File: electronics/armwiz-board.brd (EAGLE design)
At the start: 98.8 x 51 mm, 85 parts, among them IC1 MCP3424, J1 SD_MICRO_SDIO_1BIT, J2 CORTEX_DEBUGSMD, U1 STM32F10XRXT6, U4 MIC5219-3.3V, X2 M12_BOTTOM_CONTACTS_FPC_1MM, Y1 32.768kHz, Y3 32.768kHz

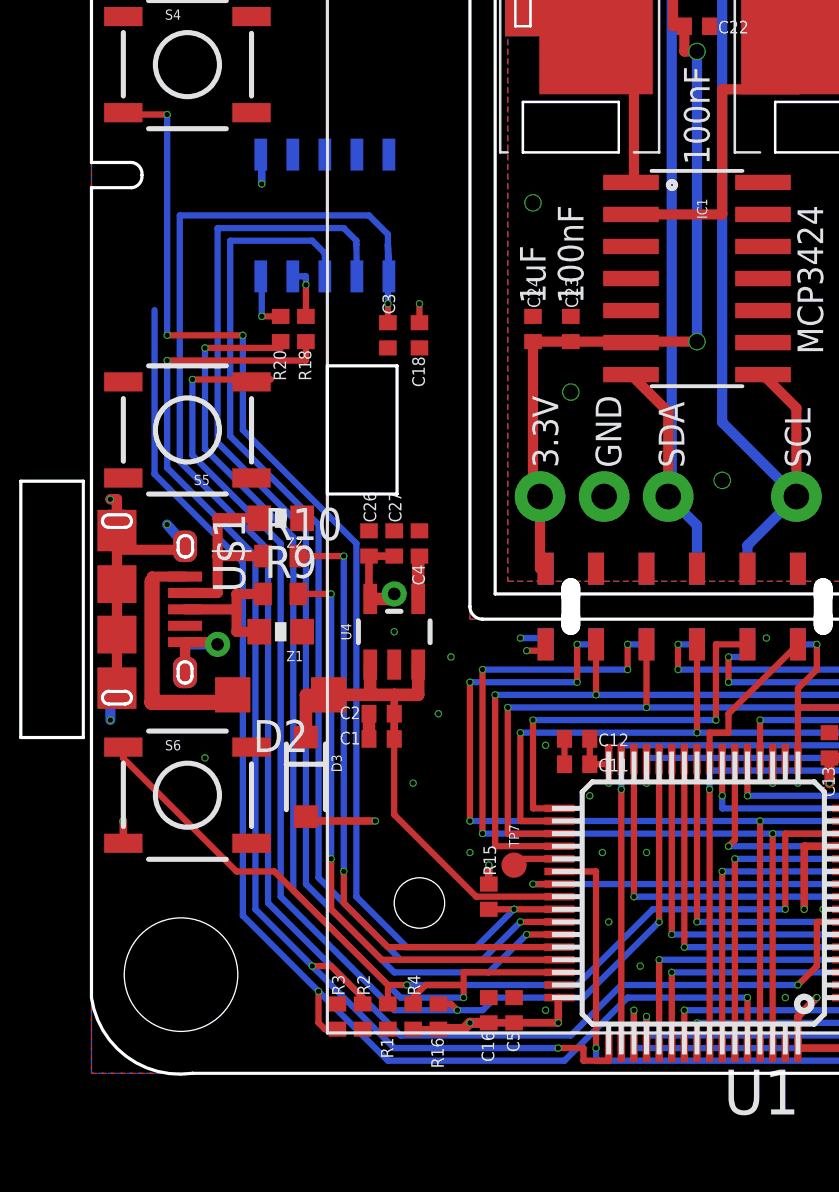
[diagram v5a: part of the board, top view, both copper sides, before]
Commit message: Changed serial pins on Cortex header. Added SWO to Cortex header. Added TODO notes to schematic.
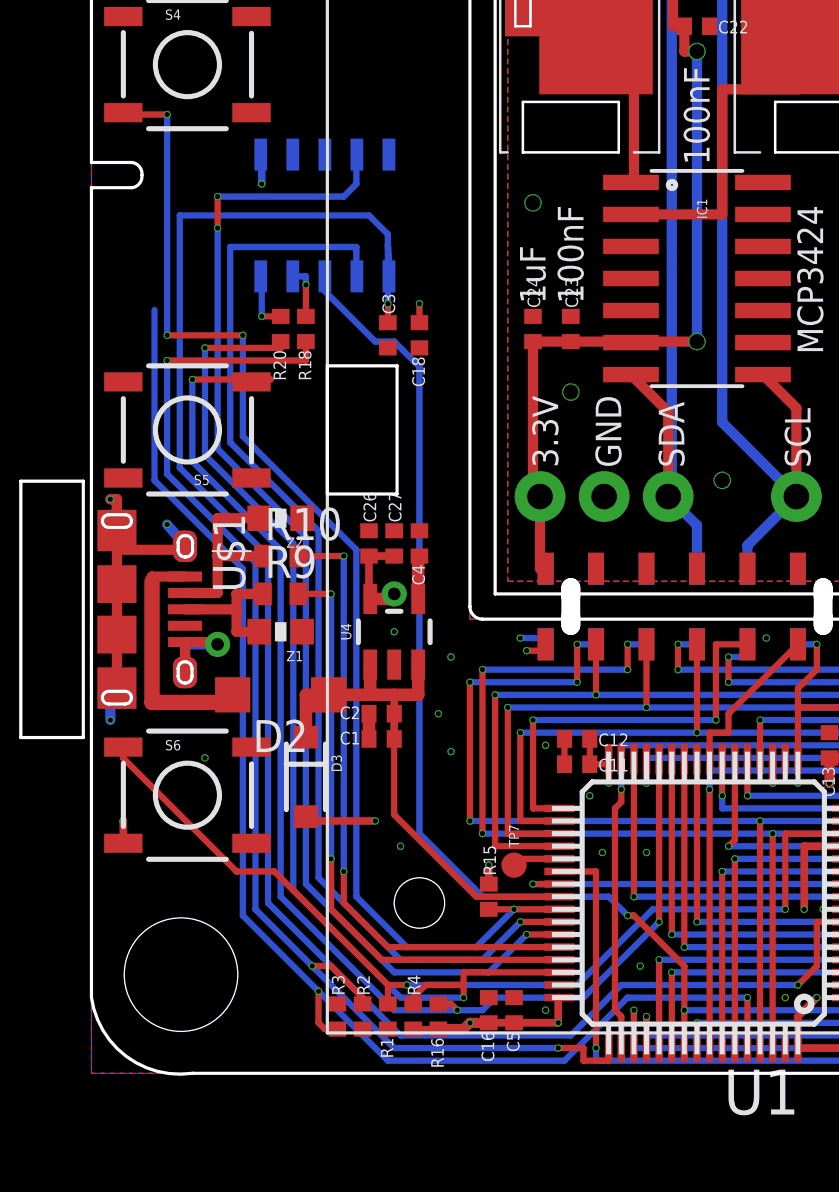
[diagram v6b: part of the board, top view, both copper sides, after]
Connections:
- removed net LCD_SCK_(SPI3_SCK): U1.55, X2.7
- new net LCD_SCK_(SPI3_SCK_SWO): J2.6, U1.55, X2.7
- net USART1_RX: now also J2.7; no longer J2.8
- net USART1_TX: now also J2.8; no longer J2.6
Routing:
- net LCD_SCK_(SPI3_SCK_SWO): track 0.00 -> 75.8 mm, vias 0 -> 3
- net LCD_SCK_(SPI3_SCK): track 37.2 -> 0.00 mm, vias 2 -> 0
- net USART1_TX: track 43.1 -> 44.1 mm
- net USART1_RX: track 46.7 -> 47.7 mm, vias 1 -> 3
- net GND: vias 83 -> 82
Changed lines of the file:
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@@
 <wire x1="11" y1="14.25" x2="11" y2="13.25" width="0.5" layer="1"/>
 <via x="21.75" y="4.25" extent="1-16" drill="0.2"/>
-<via x="20.5" y="6" extent="1-16" drill="0.2"/>
-<via x="12.75" y="11.5" extent="1-16" drill="0.2"/>
+<via x="14.25" y="12.75" extent="1-16" drill="0.2"/>
 <via x="18" y="2.5" extent="1-16" drill="0.2"/>
 <contactref element="R3" pad="1"/>
@@
 <via x="84.5" y="40.5" extent="1-16" drill="0.2"/>
 <via x="89.25" y="43.75" extent="1-16" drill="0.2"/>
-<via x="15" y="8.75" extent="1-16" drill="0.2"/>
+<via x="12.25" y="9" extent="1-16" drill="0.2"/>
 <via x="13.75" y="14.25" extent="1-16" drill="0.2"/>
 <via x="12" y="17.5" extent="1-16" drill="0.2"/>
@@
 <contactref element="S4" pad="3"/>
 <contactref element="U1" pad="41"/>
-<wire x1="10.5" y1="7" x2="10.5" y2="21" width="0.25" layer="16"/>
-<wire x1="10.5" y1="21" x2="6" y2="25.5" width="0.25" layer="16"/>
-<wire x1="6" y1="25.5" x2="6" y2="29.25" width="0.25" layer="16"/>
+<wire x1="10.5" y1="7" x2="10.5" y2="20.75" width="0.25" layer="16"/>
+<wire x1="10.5" y1="20.75" x2="6" y2="25.25" width="0.25" layer="16"/>
+<wire x1="6" y1="25.25" x2="6" y2="29.25" width="0.25" layer="16"/>
 <wire x1="18.55" y1="6.5" x2="16.75" y2="6.5" width="0.25" layer="1"/>
 <via x="16.75" y="6.5" extent="1-16" drill="0.2"/>
@@
 <wire x1="19" y1="1.5" x2="12.25" y2="1.5" width="0.25" layer="16"/>
 <wire x1="12.25" y1="1.5" x2="7" y2="6.75" width="0.25" layer="16"/>
-<wire x1="7" y1="6.75" x2="7" y2="20.75" width="0.25" layer="16"/>
-<wire x1="7" y1="20.75" x2="3.5" y2="24.25" width="0.25" layer="16"/>
-<wire x1="3.5" y1="24.25" x2="3.5" y2="34" width="0.25" layer="16"/>
+<wire x1="7" y1="6.75" x2="7" y2="20.5" width="0.25" layer="16"/>
+<wire x1="7" y1="20.5" x2="3.5" y2="24" width="0.25" layer="16"/>
+<wire x1="3.5" y1="24" x2="3.5" y2="34" width="0.25" layer="16"/>
 <wire x1="11.75" y1="29.75" x2="11.75" y2="30.5" width="0.25" layer="1"/>
 <via x="11.75" y="30.5" extent="1-16" drill="0.2"/>
@@
 <wire x1="14.75" y1="3" x2="12.25" y2="3" width="0.25" layer="16"/>
 <wire x1="12.25" y1="3" x2="8" y2="7.25" width="0.25" layer="16"/>
-<wire x1="8" y1="7.25" x2="8" y2="21.25" width="0.25" layer="16"/>
-<wire x1="8" y1="21.25" x2="4.5" y2="24.75" width="0.25" layer="16"/>
-<wire x1="4.5" y1="24.75" x2="4.5" y2="28.75" width="0.25" layer="16"/>
+<wire x1="8" y1="7.25" x2="8" y2="21" width="0.25" layer="16"/>
+<wire x1="8" y1="21" x2="4.5" y2="24.5" width="0.25" layer="16"/>
+<wire x1="4.5" y1="24.5" x2="4.5" y2="28.75" width="0.25" layer="16"/>
 <via x="4.5" y="28.75" extent="1-16" drill="0.2"/>
 <wire x1="12.75" y1="2.75" x2="12.75" y2="3" width="0.25" layer="1"/>
@@
 <wire x1="15.5" y1="4.5" x2="12.25" y2="4.5" width="0.25" layer="16"/>
 <wire x1="12.25" y1="4.5" x2="9" y2="7.75" width="0.25" layer="16"/>
-<wire x1="9" y1="7.75" x2="9" y2="21.75" width="0.25" layer="16"/>
-<wire x1="9" y1="21.75" x2="5.5" y2="25.25" width="0.25" layer="16"/>
-<wire x1="5.5" y1="25.25" x2="5.5" y2="33" width="0.25" layer="16"/>
+<wire x1="9" y1="7.75" x2="9" y2="21.5" width="0.25" layer="16"/>
+<wire x1="9" y1="21.5" x2="5.5" y2="25" width="0.25" layer="16"/>
+<wire x1="5.5" y1="25" x2="5.5" y2="32.75" width="0.25" layer="16"/>
 <via x="17" y="6" extent="1-16" drill="0.2"/>
-<contactref element="J2" pad="6"/>
-<wire x1="5.5" y1="33" x2="8.75" y2="33" width="0.25" layer="16"/>
-<wire x1="8.75" y1="33" x2="9.25" y2="32.5" width="0.25" layer="16"/>
-<wire x1="9.25" y1="32.5" x2="9.25" y2="31.587" width="0.25" layer="16"/>
+<contactref element="J2" pad="8"/>
+<wire x1="5.5" y1="32.75" x2="10.5" y2="32.75" width="0.254" layer="16"/>
+<wire x1="10.5" y1="32.75" x2="10.5" y2="31.607" width="0.254" layer="16"/>
+<wire x1="10.5" y1="31.607" x2="10.52" y2="31.587" width="0.254" layer="16"/>
 </signal>
 <signal name="USART1_RX">
@@
 <wire x1="15.75" y1="4" x2="12" y2="4" width="0.25" layer="16"/>
 <wire x1="12" y1="4" x2="8.5" y2="7.5" width="0.25" layer="16"/>
-<wire x1="8.5" y1="7.5" x2="8.5" y2="21.5" width="0.25" layer="16"/>
-<wire x1="8.5" y1="21.5" x2="5" y2="25" width="0.25" layer="16"/>
-<wire x1="5" y1="25" x2="5" y2="33.5" width="0.25" layer="16"/>
+<wire x1="8.5" y1="7.5" x2="8.5" y2="21.25" width="0.25" layer="16"/>
+<wire x1="8.5" y1="21.25" x2="5" y2="24.75" width="0.25" layer="16"/>
+<wire x1="5" y1="24.75" x2="5" y2="33.5" width="0.25" layer="16"/>
 <via x="17.25" y="5.5" extent="1-16" drill="0.2"/>
-<contactref element="J2" pad="8"/>
-<wire x1="5" y1="33.5" x2="10" y2="33.5" width="0.25" layer="16"/>
-<wire x1="10" y1="33.5" x2="10.5" y2="33" width="0.25" layer="16"/>
-<wire x1="10.5" y1="33" x2="10.5" y2="32.837" width="0.25" layer="16"/>
-<wire x1="10.5" y1="32.837" x2="10.52" y2="31.587" width="0.25" layer="16"/>
+<contactref element="J2" pad="7"/>
+<via x="5" y="33.5" extent="1-16" drill="0.2"/>
+<wire x1="5" y1="33.5" x2="5" y2="34.75" width="0.254" layer="1"/>
+<via x="5" y="34.75" extent="1-16" drill="0.2"/>
+<wire x1="5" y1="34.75" x2="10" y2="34.75" width="0.254" layer="16"/>
+<wire x1="10" y1="34.75" x2="10.5" y2="35.25" width="0.254" layer="16"/>
+<wire x1="10.5" y1="35.25" x2="10.5" y2="36.393" width="0.254" layer="16"/>
+<wire x1="10.5" y1="36.393" x2="10.52" y2="36.413" width="0.254" layer="16"/>
 </signal>
 <signal name="N$13">
@@
 <wire x1="38" y1="16.5" x2="38.75" y2="16.5" width="0.25" layer="16"/>
 </signal>
-<signal name="LCD_SCK_(SPI3_SCK)">
+<signal name="LCD_SCK_(SPI3_SCK_SWO)">
 <contactref element="U1" pad="55"/>
 <wire x1="23.5" y1="2.5" x2="48.5" y2="2.5" width="0.25" layer="16"/>
@@
 <wire x1="23.5" y1="1.05" x2="23.5" y2="2.5" width="0.25" layer="1"/>
 <via x="23.5" y="2.5" extent="1-16" drill="0.2"/>
+<contactref element="J2" pad="6"/>
+<wire x1="23.5" y1="2.5" x2="23.5" y2="4.25" width="0.254" layer="1"/>
+<wire x1="23.5" y1="4.25" x2="21.5" y2="6.25" width="0.254" layer="1"/>
+<wire x1="21.5" y1="6.25" x2="21.25" y2="6.25" width="0.254" layer="1"/>
+<wire x1="9.25" y1="31.587" x2="9.25" y2="31" width="0.254" layer="16"/>
+<wire x1="9.25" y1="31" x2="11.25" y2="29" width="0.254" layer="16"/>
+<wire x1="11.25" y1="29" x2="12" y2="29" width="0.254" layer="16"/>
+<wire x1="12" y1="29" x2="13" y2="28" width="0.254" layer="16"/>
+<wire x1="13" y1="28" x2="13" y2="9.5" width="0.254" layer="16"/>
+<wire x1="13" y1="9.5" x2="15.5" y2="7" width="0.254" layer="16"/>
+<wire x1="15.5" y1="7" x2="20.5" y2="7" width="0.254" layer="16"/>
+<wire x1="20.5" y1="7" x2="21.25" y2="6.25" width="0.254" layer="16"/>
+<via x="21.25" y="6.25" extent="1-16" drill="0.2"/>
 </signal>
 <signal name="LCD_MOSI_(SPI3_MOSI)">
@@
 <wire x1="12" y1="1" x2="8.75" y2="4.25" width="0.25" layer="16"/>
 <wire x1="8.75" y1="4.25" x2="6.5" y2="6.5" width="0.25" layer="16"/>
-<wire x1="6.5" y1="6.5" x2="6.5" y2="20.5" width="0.25" layer="16"/>
-<wire x1="6.5" y1="20.5" x2="3" y2="24" width="0.25" layer="16"/>
-<wire x1="3" y1="24" x2="3" y2="28.25" width="0.25" layer="16"/>
+<wire x1="6.5" y1="6.5" x2="6.5" y2="20.25" width="0.25" layer="16"/>
+<wire x1="6.5" y1="20.25" x2="3" y2="23.75" width="0.25" layer="16"/>
+<wire x1="3" y1="23.75" x2="3" y2="28.25" width="0.25" layer="16"/>
 <via x="3" y="28.25" extent="1-16" drill="0.2"/>
 <wire x1="8.5" y1="28.25" x2="8.5" y2="29" width="0.25" layer="1"/>
@@
 <signal name="LCD_CS_(SPI3_NSS)">
 <contactref element="U1" pad="50"/>
-<wire x1="21" y1="1.05" x2="21" y2="11.25" width="0.25" layer="1"/>
+<wire x1="21" y1="1.05" x2="21" y2="2.25" width="0.25" layer="1"/>
+<wire x1="21" y1="2.25" x2="20.75" y2="2.5" width="0.25" layer="1"/>
+<wire x1="20.75" y1="2.5" x2="20.75" y2="10.5" width="0.25" layer="1"/>
+<wire x1="20.75" y1="10.5" x2="21" y2="10.75" width="0.25" layer="1"/>
+<wire x1="21" y1="10.75" x2="21" y2="11.25" width="0.25" layer="1"/>
 <via x="21" y="11.25" extent="1-16" drill="0.2"/>
 <via x="51.5" y="12" extent="1-16" drill="0.2"/>
@@
 <wire x1="14.5" y1="2.5" x2="12" y2="2.5" width="0.25" layer="16"/>
 <wire x1="12" y1="2.5" x2="7.5" y2="7" width="0.25" layer="16"/>
-<wire x1="7.5" y1="7" x2="7.5" y2="21" width="0.25" layer="16"/>
-<wire x1="7.5" y1="21" x2="4" y2="24.5" width="0.25" layer="16"/>
-<wire x1="4" y1="24.5" x2="4" y2="27.5" width="0.25" layer="16"/>
+<wire x1="7.5" y1="7" x2="7.5" y2="20.75" width="0.25" layer="16"/>
+<wire x1="7.5" y1="20.75" x2="4" y2="24.25" width="0.25" layer="16"/>
+<wire x1="4" y1="24.25" x2="4" y2="27.5" width="0.25" layer="16"/>
 <via x="14.5" y="2.5" extent="1-16" drill="0.2"/>
 <wire x1="6.344" y1="27.405" x2="7.094" y2="27.5" width="0.25" layer="1"/>
@@
 <contactref element="R3" pad="2"/>
 <wire x1="9" y1="3.25" x2="6" y2="6.25" width="0.25" layer="16"/>
-<wire x1="6" y1="6.25" x2="6" y2="20.25" width="0.25" layer="16"/>
-<wire x1="6" y1="20.25" x2="2.5" y2="23.75" width="0.25" layer="16"/>
-<wire x1="2.5" y1="23.75" x2="2.5" y2="30.25" width="0.25" layer="16"/>
+<wire x1="6" y1="6.25" x2="6" y2="20" width="0.25" layer="16"/>
+<wire x1="6" y1="20" x2="2.5" y2="23.5" width="0.25" layer="16"/>
+<wire x1="2.5" y1="23.5" x2="2.5" y2="30.25" width="0.25" layer="16"/>
 <wire x1="9.75" y1="1.75" x2="9.25" y2="1.75" width="0.25" layer="1"/>
 <wire x1="9.25" y1="1.75" x2="9" y2="2" width="0.25" layer="1"/>

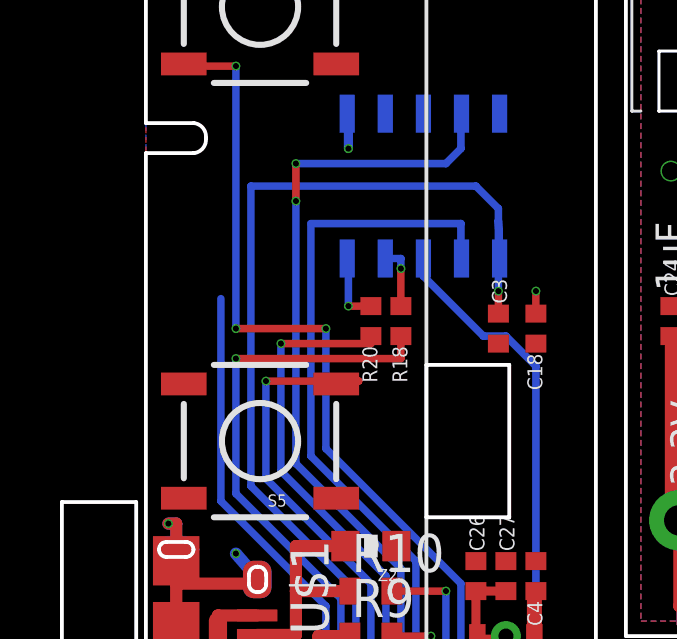
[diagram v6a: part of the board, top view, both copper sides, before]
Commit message: Added pogo pin pads for SWD.
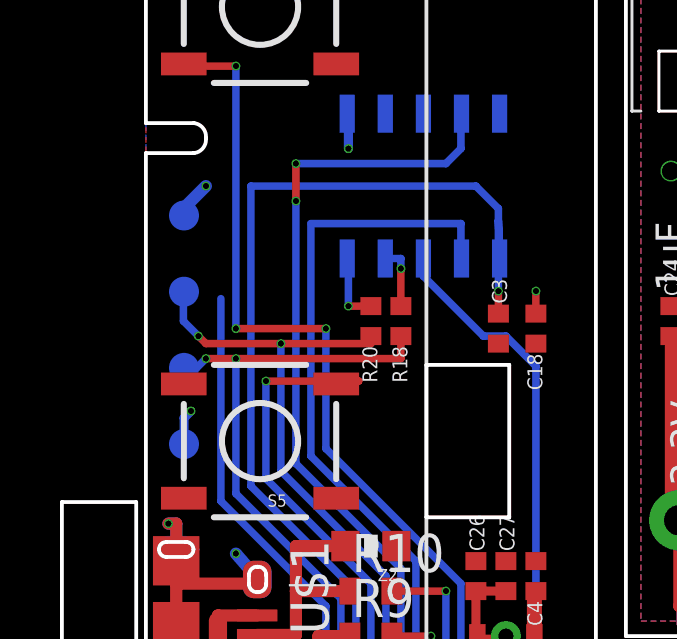
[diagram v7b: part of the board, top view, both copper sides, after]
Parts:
- added TP5, TP6, TP8, TP9: (no value), PaxInstruments-Connectors:PAD_1MM
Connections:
- net 3.3V: now also TP8.P$1
- net GND: now also TP9.P$1
- net SWCLK: now also TP6.P$1
- net SWDIO: now also TP5.P$1
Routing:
- net SWDIO: track 42.0 -> 46.6 mm, vias 2 -> 3
- net SWCLK: track 49.7 -> 51.6 mm, vias 3 -> 4
- net 3.3V: track 60.0 -> 61.3 mm, vias 24 -> 25
- net GND: track 25.6 -> 26.8 mm, vias 82 -> 83
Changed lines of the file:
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@@
 <layer number="23" name="tOrigins" color="15" fill="1" visible="yes" active="yes"/>
 <layer number="24" name="bOrigins" color="15" fill="1" visible="yes" active="yes"/>
-<layer number="25" name="tNames" color="7" fill="1" visible="yes" active="yes"/>
-<layer number="26" name="bNames" color="7" fill="1" visible="yes" active="yes"/>
-<layer number="27" name="tValues" color="7" fill="1" visible="yes" active="yes"/>
-<layer number="28" name="bValues" color="7" fill="1" visible="yes" active="yes"/>
+<layer number="25" name="tNames" color="7" fill="1" visible="no" active="yes"/>
+<layer number="26" name="bNames" color="7" fill="1" visible="no" active="yes"/>
+<layer number="27" name="tValues" color="7" fill="1" visible="no" active="yes"/>
+<layer number="28" name="bValues" color="7" fill="1" visible="no" active="yes"/>
 <layer number="29" name="tStop" color="7" fill="3" visible="yes" active="yes"/>
 <layer number="30" name="bStop" color="7" fill="6" visible="yes" active="yes"/>
@@
 <layer number="42" name="bRestrict" color="1" fill="10" visible="yes" active="yes"/>
 <layer number="43" name="vRestrict" color="2" fill="10" visible="yes" active="yes"/>
-<layer number="44" name="Drills" color="7" fill="1" visible="yes" active="yes"/>
-<layer number="45" name="Holes" color="7" fill="1" visible="yes" active="yes"/>
+<layer number="44" name="Drills" color="7" fill="1" visible="no" active="yes"/>
+<layer number="45" name="Holes" color="7" fill="1" visible="no" active="yes"/>
 <layer number="46" name="Milling" color="3" fill="1" visible="yes" active="yes"/>
 <layer number="47" name="Measures" color="7" fill="1" visible="yes" active="yes"/>
@@
 </element>
 <element name="U$8" library="PaxInstruments-Aesthetics" package="PAX-LOGO-0.25IN" value="0.25 in" x="25" y="29.5" rot="MR0"/>
+<element name="TP5" library="PaxInstruments-Connectors" package="PAD_1MM" value="" x="1.27" y="30.48" rot="MR0"/>
+<element name="TP6" library="PaxInstruments-Connectors" package="PAD_1MM" value="" x="1.27" y="27.94" rot="MR0"/>
+<element name="TP8" library="PaxInstruments-Connectors" package="PAD_1MM" value="" x="1.27" y="33.02" rot="MR0"/>
+<element name="TP9" library="PaxInstruments-Connectors" package="PAD_1MM" value="" x="1.27" y="25.4" rot="MR0"/>
 </elements>
 <signals>
@@
 <wire x1="6.71" y1="36.413" x2="6.75" y2="36.413" width="0.3048" layer="16"/>
 <wire x1="6.75" y1="36.413" x2="6.75" y2="35.25" width="0.3048" layer="16"/>
+<contactref element="TP8" pad="P$1"/>
+<wire x1="1.27" y1="33.02" x2="1.27" y2="33.27" width="0.4064" layer="16"/>
+<wire x1="1.27" y1="33.27" x2="2" y2="34" width="0.4064" layer="16"/>
+<via x="2" y="34" extent="1-16" drill="0.2"/>
 </signal>
 <signal name="GND" class="5">
@@
 <via x="12" y="17.5" extent="1-16" drill="0.2"/>
 <via x="4.5" y="12.5" extent="1-16" drill="0.2"/>
+<contactref element="TP9" pad="P$1"/>
+<wire x1="1.27" y1="25.4" x2="1.27" y2="26.27" width="0.3" layer="16"/>
+<wire x1="1.27" y1="26.27" x2="1.5" y2="26.5" width="0.3" layer="16"/>
+<via x="1.5" y="26.5" extent="1-16" drill="0.2"/>
 </signal>
 <signal name="N$3">
@@
 <wire x1="4.5" y1="28.75" x2="7.5" y2="28.75" width="0.25" layer="1"/>
 <wire x1="7.5" y1="28.75" x2="7.5" y2="29" width="0.25" layer="1"/>
+<contactref element="TP5" pad="P$1"/>
+<wire x1="1.27" y1="30.48" x2="1.25" y2="30.5" width="0.25" layer="16"/>
+<wire x1="1.25" y1="30.5" x2="1.25" y2="29.5" width="0.25" layer="16"/>
+<wire x1="1.25" y1="29.5" x2="1.75" y2="29" width="0.25" layer="16"/>
+<via x="1.75" y="29" extent="1-16" drill="0.2"/>
+<wire x1="1.75" y1="29" x2="2" y2="28.75" width="0.25" layer="1"/>
+<wire x1="2" y1="28.75" x2="4.5" y2="28.75" width="0.25" layer="1"/>
 </signal>
 <signal name="LCD_A0_(GPIO)">
@@
 <via x="8.75" y="4.25" extent="1-16" drill="0.2"/>
 <wire x1="8.75" y1="4.25" x2="8.875" y2="4.125" width="0.25" layer="16"/>
+<contactref element="TP6" pad="P$1"/>
+<wire x1="1.27" y1="27.94" x2="1.69" y2="27.94" width="0.25" layer="16"/>
+<wire x1="1.69" y1="27.94" x2="2" y2="28.25" width="0.25" layer="16"/>
+<via x="2" y="28.25" extent="1-16" drill="0.2"/>
+<wire x1="2" y1="28.25" x2="3" y2="28.25" width="0.25" layer="1"/>
 </signal>
 <signal name="GPIO_(SPI2_NSS)">
